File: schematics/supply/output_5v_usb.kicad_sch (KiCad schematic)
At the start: 90 parts, among them J2 USB_A, Q1 40N06, Q2 STP13NK60Z, Q3 STP13NK60Z, U1 INA3221, U10 LM158DR, U11 LM1085-3.3, U2 EL817, U3 MC34063AD, U4 L78L33ACUTR, U5 IRS2153S, U6 LM158DR, U7 IP2163, U8 LM158DR, U9 TL432DBZ

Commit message: Found and fixed issues in schematics.
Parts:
- added R64: 0.01, Resistor_SMD:R_2512_6332Metric, symbol Device:R
- C7: value 0.33 uF -> 10 uF
- C9: value 100 nF -> 10 uF
- R10, R9: value 5 -> 10
- R13, R18, R23, R24: value 1K -> 510
- R6: value 1K -> 50
- U5: value IRS2153S -> IR2153S
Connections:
- net USB_1_+5V: now also R64.1; no longer L1.1, U3.1 (SwC), U3.7 (Ipk), U3.8 (DC)
- new net: L1.1, R64.2, U3.1 (SwC), U3.7 (Ipk), U3.8 (DC)
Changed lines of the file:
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@@
   (junction (at 304.8 33.02) (diameter 0) (color 0 0 0 0)
   )
-  (junction (at 76.2 144.78) (diameter 0) (color 0 0 0 0)
-  )
   (junction (at 85.09 59.69) (diameter 0) (color 0 0 0 0)
   )
@@
   (junction (at 382.27 160.02) (diameter 0) (color 0 0 0 0)
   )
+  (junction (at 76.2 139.7) (diameter 0) (color 0 0 0 0)
+  )
   (junction (at 120.65 193.04) (diameter 0) (color 0 0 0 0)
   )
@@
   (junction (at 187.96 48.26) (diameter 0) (color 0 0 0 0)
   )
+  (junction (at 76.2 142.24) (diameter 0) (color 0 0 0 0)
+  )
   (junction (at 152.4 41.91) (diameter 0) (color 0 0 0 0)
   )
@@
   (junction (at 275.59 48.26) (diameter 0) (color 0 0 0 0)
   )
+  (junction (at 87.63 139.7) (diameter 0) (color 0 0 0 0)
+  )
   (junction (at 337.82 102.87) (diameter 0) (color 0 0 0 0)
   )
@@
   (junction (at 347.98 156.21) (diameter 0) (color 0 0 0 0)
   )
-  (junction (at 87.63 139.7) (diameter 0) (color 0 0 0 0)
-  )
   (junction (at 85.09 45.72) (diameter 0) (color 0 0 0 0)
   )
@@
     (stroke (width 0) (type default))
   )
-  (wire (pts (xy 76.2 139.7) (xy 87.63 139.7))
-    (stroke (width 0) (type default))
-  )
   (wire (pts (xy 31.75 236.22) (xy 36.83 236.22))
     (stroke (width 0) (type default))
@@
     (stroke (width 0) (type default))
   )
+  (wire (pts (xy 76.2 139.7) (xy 76.2 142.24))
+    (stroke (width 0) (type default))
+  )
   (wire (pts (xy 381 64.77) (xy 391.16 64.77))
     (stroke (width 0) (type default))
@@
     (stroke (width 0) (type default))
   )
+  (wire (pts (xy 87.63 137.16) (xy 87.63 139.7))
+    (stroke (width 0) (type default))
+  )
   (wire (pts (xy 113.03 233.68) (xy 113.03 234.95))
     (stroke (width 0) (type default))
@@
     (stroke (width 0) (type default))
   )
-  (wire (pts (xy 87.63 139.7) (xy 97.79 139.7))
+  (wire (pts (xy 76.2 139.7) (xy 87.63 139.7))
     (stroke (width 0) (type default))
   )
@@
     (stroke (width 0) (type default))
   )
-  (wire (pts (xy 76.2 144.78) (xy 80.01 144.78))
-    (stroke (width 0) (type default))
-  )
   (wire (pts (xy 250.19 52.07) (xy 250.19 48.26))
     (stroke (width 0) (type default))
@@
     (stroke (width 0) (type default))
   )
+  (wire (pts (xy 87.63 127) (xy 87.63 129.54))
+    (stroke (width 0) (type default))
+  )
   (wire (pts (xy 388.62 86.36) (xy 388.62 88.9))
     (stroke (width 0) (type default))
@@
     (stroke (width 0) (type default))
   )
+  (wire (pts (xy 87.63 139.7) (xy 97.79 139.7))
+    (stroke (width 0) (type default))
+  )
   (wire (pts (xy 187.96 33.02) (xy 187.96 35.56))
     (stroke (width 0) (type default))
@@
     (stroke (width 0) (type default))
   )
-  (wire (pts (xy 87.63 127) (xy 87.63 139.7))
-    (stroke (width 0) (type default))
-  )
   (wire (pts (xy 121.92 58.42) (xy 125.73 58.42))
     (stroke (width 0) (type default))
@@
     (effects (font (size 1.27 1.27)) (justify right bottom))
   )
-  (label "USB_1_+5V" (at 80.01 144.78 0) (fields_autoplaced)
-    (effects (font (size 1.27 1.27)) (justify left bottom))
-  )
   (hierarchical_label "+5V_OUT" (shape input) (at 31.75 45.72 180) (fields_autoplaced)
     (effects (font (size 1.27 1.27)) (justify right))
@@
       (effects (font (size 1.27 1.27)) (justify left))
     )
-    (property "Value" "IRS2153S" (at 96.52 29.21 0)
+    (property "Value" "IR2153S" (at 96.52 29.21 0)
       (effects (font (size 1.27 1.27)) (justify left))
     )
@@
   (symbol (lib_id "Device:R") (at 129.54 58.42 90) (unit 1)
     (in_bom yes) (on_board yes) (dnp no) (fields_autoplaced)
-    (property "Reference" "R10" (at 129.54 53.34 90)
+    (property "Reference" "R10" (at 129.54 52.07 90)
       (effects (font (size 1.27 1.27)))
     )
-    (property "Value" "5" (at 129.54 55.88 90)
+    (property "Value" "10" (at 129.54 54.61 90)
       (effects (font (size 1.27 1.27)))
     )
@@
       (effects (font (size 1.27 1.27)) (justify right))
     )
-    (property "Value" "0.33 uF" (at 80.01 231.14 0)
+    (property "Value" "10 uF" (at 80.01 231.14 0)
       (effects (font (size 1.27 1.27)) (justify right))
     )
@@
   (symbol (lib_id "Device:R") (at 180.34 260.35 90) (unit 1)
     (in_bom yes) (on_board yes) (dnp no) (fields_autoplaced)
-    (property "Reference" "R13" (at 180.34 255.27 90)
+    (property "Reference" "R13" (at 180.34 254 90)
       (effects (font (size 1.27 1.27)))
     )
-    (property "Value" "1K" (at 180.34 257.81 90)
+    (property "Value" "510" (at 180.34 256.54 90)
       (effects (font (size 1.27 1.27)))
     )
@@
       (effects (font (size 1.27 1.27)) (justify right))
     )
-    (property "Value" "100 nF" (at 116.84 231.14 0)
+    (property "Value" "10 uF" (at 116.84 231.14 0)
       (effects (font (size 1.27 1.27)) (justify right))
     )
@@
   (symbol (lib_id "Device:R") (at 279.4 200.66 90) (unit 1)
     (in_bom yes) (on_board yes) (dnp no) (fields_autoplaced)
-    (property "Reference" "R18" (at 279.4 195.58 90)
+    (property "Reference" "R18" (at 279.4 194.31 90)
       (effects (font (size 1.27 1.27)))
     )
-    (property "Value" "1K" (at 279.4 198.12 90)
+    (property "Value" "510" (at 279.4 196.85 90)
       (effects (font (size 1.27 1.27)))
     )
@@
       (effects (font (size 1.27 1.27)) (justify right))
     )
-    (property "Value" "1K" (at 391.16 93.98 0)
+    (property "Value" "510" (at 391.16 93.98 0)
       (effects (font (size 1.27 1.27)) (justify right))
     )
@@
   (symbol (lib_id "Device:R") (at 129.54 26.67 90) (unit 1)
     (in_bom yes) (on_board yes) (dnp no) (fields_autoplaced)
-    (property "Reference" "R9" (at 129.54 21.59 90)
+    (property "Reference" "R9" (at 129.54 20.32 90)
       (effects (font (size 1.27 1.27)))
     )
-    (property "Value" "5" (at 129.54 24.13 90)
+    (property "Value" "10" (at 129.54 22.86 90)
       (effects (font (size 1.27 1.27)))
     )
@@
   (symbol (lib_id "Device:R") (at 99.06 154.94 0) (unit 1)
     (in_bom yes) (on_board yes) (dnp no) (fields_autoplaced)
-    (property "Reference" "R6" (at 101.6 154.305 0)
+    (property "Reference" "R6" (at 101.6 153.67 0)
       (effects (font (size 1.27 1.27)) (justify left))
     )
-    (property "Value" "1K" (at 101.6 156.845 0)
+    (property "Value" "50" (at 101.6 156.21 0)
       (effects (font (size 1.27 1.27)) (justify left))
     )
@@
     )
   )
+  (symbol (lib_id "Device:R") (at 87.63 133.35 0) (unit 1)
+    (in_bom yes) (on_board yes) (dnp no)
+    (property "Reference" "R64" (at 83.82 132.08 0)
+      (effects (font (size 1.27 1.27)))
+    )
+    (property "Value" "0.01" (at 83.82 134.62 0)
+      (effects (font (size 1.27 1.27)))
+    )
+    (property "Footprint" "Resistor_SMD:R_2512_6332Metric" (at 85.852 133.35 90)
+      (effects (font (size 1.27 1.27)) hide)
+    )
+    (property "Datasheet" "~" (at 87.63 133.35 0)
+      (effects (font (size 1.27 1.27)) hide)
+    )
+    (pin "1")
+    (pin "2")
+    (instances
+      (project "supply"
+        (path "/1e139717-fcd1-4008-a6ea-4c993845e928/bcabd54f-a555-4409-9a4f-89c20a3d7682"
+          (reference "R64") (unit 1)
+        )
+      )
+    )
+  )
   (symbol (lib_id "power:GND") (at 275.59 101.6 0) (unit 1)
     (in_bom yes) (on_board yes) (dnp no) (fields_autoplaced)
@@
   (symbol (lib_id "Device:R") (at 350.52 200.66 90) (unit 1)
     (in_bom yes) (on_board yes) (dnp no) (fields_autoplaced)
-    (property "Reference" "R23" (at 350.52 195.58 90)
+    (property "Reference" "R23" (at 350.52 194.31 90)
       (effects (font (size 1.27 1.27)))
     )
-    (property "Value" "1K" (at 350.52 198.12 90)
+    (property "Value" "510" (at 350.52 196.85 90)
       (effects (font (size 1.27 1.27)))
     )

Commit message: Some changes
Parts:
- C4: value 100 nF -> 1 uF
- R1: value 510 -> 120
- R17: value 10K -> 3K3
- R2: value 1K2 -> NOT INSTALLED
- R6: value 50 -> 51
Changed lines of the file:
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@@
       (effects (font (size 1.27 1.27)) (justify right))
     )
-    (property "Value" "1K2" (at 50.8 53.34 0)
+    (property "Value" "NOT INSTALLED" (at 50.8 53.34 0)
       (effects (font (size 1.27 1.27)) (justify right))
     )
@@
       (effects (font (size 1.27 1.27)) (justify left))
     )
-    (property "Value" "10K" (at 278.13 93.98 0)
+    (property "Value" "3K3" (at 278.13 93.98 0)
       (effects (font (size 1.27 1.27)) (justify left))
     )
@@
       (effects (font (size 1.27 1.27) italic) hide)
     )
-    (property "Datasheet" "http://www.ti.com/lit/ds/symlink/lm1085.pdf" (at 353.06 102.87 0)
+    (property "Datasheet" "https://static.chipdip.ru/lib/142/DOC000142627.pdf" (at 353.06 102.87 0)
       (effects (font (size 1.27 1.27)) hide)
     )
@@
   (symbol (lib_id "Device:R") (at 39.37 45.72 270) (mirror x) (unit 1)
     (in_bom yes) (on_board yes) (dnp no) (fields_autoplaced)
-    (property "Reference" "R1" (at 39.37 40.64 90)
-      (effects (font (size 1.27 1.27)))
-    )
-    (property "Value" "510" (at 39.37 43.18 90)
+    (property "Reference" "R1" (at 39.37 39.37 90)
+      (effects (font (size 1.27 1.27)))
+    )
+    (property "Value" "120" (at 39.37 41.91 90)
       (effects (font (size 1.27 1.27)))
     )
@@
       (effects (font (size 1.27 1.27)) (justify left))
     )
-    (property "Value" "50" (at 101.6 156.21 0)
+    (property "Value" "51" (at 101.6 156.21 0)
       (effects (font (size 1.27 1.27)) (justify left))
     )
@@
       (effects (font (size 1.27 1.27)) (justify right))
     )
-    (property "Value" "100 nF" (at 74.93 26.67 0)
+    (property "Value" "1 uF" (at 74.93 26.67 0)
       (effects (font (size 1.27 1.27)) (justify right))
     )
@@
       (effects (font (size 1.27 1.27)) hide)
     )
-    (property "Datasheet" "~" (at 204.47 48.26 0)
-      (effects (font (size 1.27 1.27)) hide)
-    )
+    (property "Datasheet" "https://static.chipdip.ru/lib/926/DOC012926706.pdf" (at 204.47 48.26 0)
+      (effects (font (size 1.27 1.27)) hide)
+    )

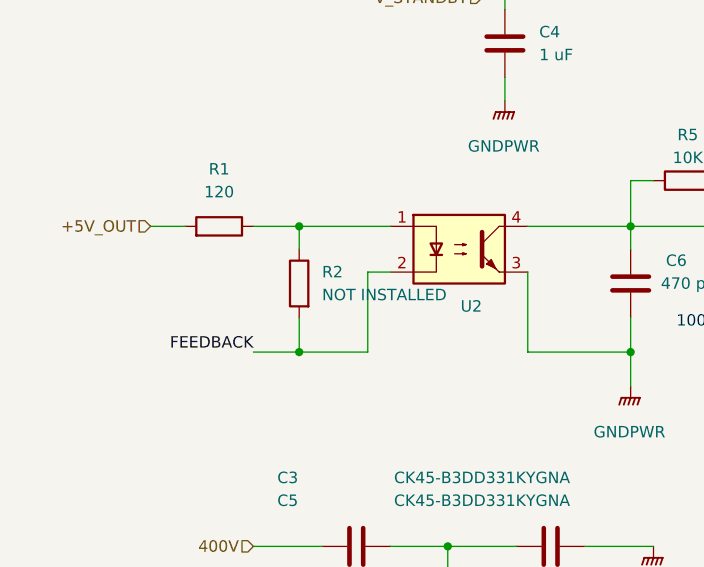
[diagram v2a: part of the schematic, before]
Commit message: fix pins in firmware
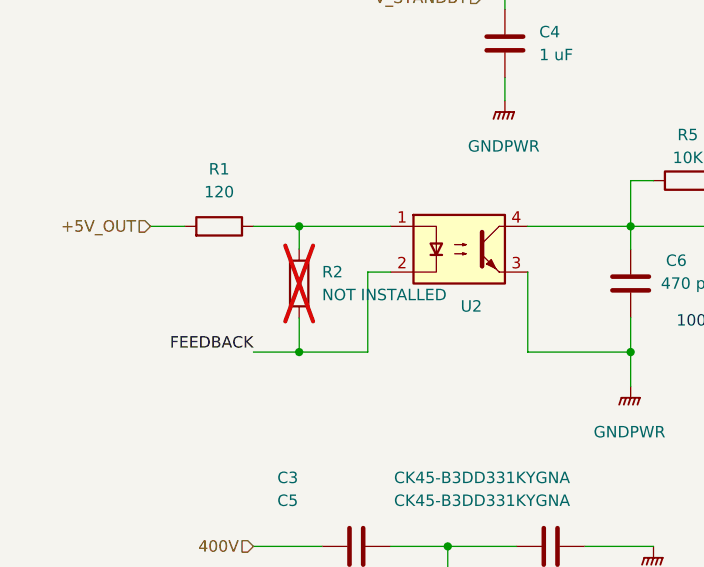
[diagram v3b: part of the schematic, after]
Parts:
- R2: now not fitted
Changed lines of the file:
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@@
   )
   (symbol (lib_id "Device:R") (at 48.26 52.07 0) (mirror y) (unit 1)
-    (in_bom yes) (on_board yes) (dnp no) (fields_autoplaced)
+    (in_bom yes) (on_board yes) (dnp yes) (fields_autoplaced)
     (property "Reference" "R2" (at 50.8 50.8 0)
       (effects (font (size 1.27 1.27)) (justify right))

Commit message: Continue soldering and setting up hardware
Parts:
- D16: value SS16 -> STTH1R06A
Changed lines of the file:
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@@
   (symbol (lib_id "Device:D") (at 115.57 26.67 180) (unit 1)
     (in_bom yes) (on_board yes) (dnp no) (fields_autoplaced)
-    (property "Reference" "D16" (at 115.57 21.59 0)
+    (property "Reference" "D16" (at 115.57 20.32 0)
       (effects (font (size 1.27 1.27)))
     )
-    (property "Value" "SS16" (at 115.57 24.13 0)
+    (property "Value" "STTH1R06A" (at 115.57 22.86 0)
       (effects (font (size 1.27 1.27)))
     )

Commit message: Board fixes
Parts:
- added R65, R66: 0.07, Resistor_SMD:R_2512_6332Metric, symbol Device:R
- R64: value 0.01 -> 0.07
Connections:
- net USB_1_+5V: now also R65.1, R66.1
- net at L1.1, R64.2, U3.1 (SwC)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: now also R65.2, R66.2
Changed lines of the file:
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@@
   (junction (at 158.75 142.24) (diameter 0) (color 0 0 0 0)
   )
+  (junction (at 91.44 128.27) (diameter 0) (color 0 0 0 0)
+  )
   (junction (at 99.06 149.86) (diameter 0) (color 0 0 0 0)
   )
@@
   (junction (at 85.09 59.69) (diameter 0) (color 0 0 0 0)
   )
+  (junction (at 87.63 128.27) (diameter 0) (color 0 0 0 0)
+  )
   (junction (at 327.66 140.97) (diameter 0) (color 0 0 0 0)
   )
@@
   (junction (at 347.98 156.21) (diameter 0) (color 0 0 0 0)
   )
+  (junction (at 87.63 138.43) (diameter 0) (color 0 0 0 0)
+  )
   (junction (at 85.09 45.72) (diameter 0) (color 0 0 0 0)
   )
   (junction (at 187.96 49.53) (diameter 0) (color 0 0 0 0)
   )
+  (junction (at 91.44 138.43) (diameter 0) (color 0 0 0 0)
+  )
   (junction (at 129.54 142.24) (diameter 0) (color 0 0 0 0)
   )
@@
     (stroke (width 0) (type default))
   )
+  (wire (pts (xy 91.44 138.43) (xy 87.63 138.43))
+    (stroke (width 0) (type default))
+  )
   (wire (pts (xy 90.17 224.79) (xy 93.98 224.79))
     (stroke (width 0) (type default))
@@
     (stroke (width 0) (type default))
   )
+  (wire (pts (xy 91.44 128.27) (xy 87.63 128.27))
+    (stroke (width 0) (type default))
+  )
   (wire (pts (xy 304.8 39.37) (xy 322.58 39.37))
     (stroke (width 0) (type default))
@@
     (stroke (width 0) (type default))
   )
-  (wire (pts (xy 87.63 137.16) (xy 87.63 139.7))
+  (wire (pts (xy 87.63 137.16) (xy 87.63 138.43))
     (stroke (width 0) (type default))
   )
@@
     (stroke (width 0) (type default))
   )
+  (wire (pts (xy 95.25 129.54) (xy 95.25 128.27))
+    (stroke (width 0) (type default))
+  )
   (wire (pts (xy 234.95 110.49) (xy 234.95 114.3))
     (stroke (width 0) (type default))
@@
     (stroke (width 0) (type default))
   )
+  (wire (pts (xy 87.63 138.43) (xy 87.63 139.7))
+    (stroke (width 0) (type default))
+  )
   (wire (pts (xy 156.21 201.93) (xy 158.75 201.93))
     (stroke (width 0) (type default))
@@
     (stroke (width 0) (type default))
   )
+  (wire (pts (xy 95.25 138.43) (xy 91.44 138.43))
+    (stroke (width 0) (type default))
+  )
   (wire (pts (xy 62.23 248.92) (xy 67.31 248.92))
     (stroke (width 0) (type default))
@@
     (stroke (width 0) (type default))
   )
+  (wire (pts (xy 95.25 137.16) (xy 95.25 138.43))
+    (stroke (width 0) (type default))
+  )
   (wire (pts (xy 73.66 45.72) (xy 85.09 45.72))
     (stroke (width 0) (type default))
@@
     (stroke (width 0) (type default))
   )
-  (wire (pts (xy 87.63 127) (xy 87.63 129.54))
+  (wire (pts (xy 87.63 127) (xy 87.63 128.27))
     (stroke (width 0) (type default))
   )
@@
     (stroke (width 0) (type default))
   )
+  (wire (pts (xy 91.44 137.16) (xy 91.44 138.43))
+    (stroke (width 0) (type default))
+  )
   (wire (pts (xy 109.22 26.67) (xy 111.76 26.67))
     (stroke (width 0) (type default))
@@
     (stroke (width 0) (type default))
   )
+  (wire (pts (xy 91.44 129.54) (xy 91.44 128.27))
+    (stroke (width 0) (type default))
+  )
   (wire (pts (xy 360.68 102.87) (xy 367.03 102.87))
     (stroke (width 0) (type default))
@@
     (stroke (width 0) (type default))
   )
+  (wire (pts (xy 87.63 128.27) (xy 87.63 129.54))
+    (stroke (width 0) (type default))
+  )
   (wire (pts (xy 229.87 114.3) (xy 223.52 114.3))
     (stroke (width 0) (type default))
@@
     (stroke (width 0) (type default))
   )
+  (wire (pts (xy 95.25 128.27) (xy 91.44 128.27))
+    (stroke (width 0) (type default))
+  )
   (wire (pts (xy 121.92 58.42) (xy 125.73 58.42))
     (stroke (width 0) (type default))
@@
     )
   )
+  (symbol (lib_id "Device:R") (at 95.25 133.35 0) (unit 1)
+    (in_bom yes) (on_board yes) (dnp no)
+    (property "Reference" "R66" (at 77.47 137.16 0)
+      (effects (font (size 1.27 1.27)))
+    )
+    (property "Value" "0.07" (at 82.55 137.16 0)
+      (effects (font (size 1.27 1.27)))
+    )
+    (property "Footprint" "Resistor_SMD:R_2512_6332Metric" (at 93.472 133.35 90)
+      (effects (font (size 1.27 1.27)) hide)
+    )
+    (property "Datasheet" "~" (at 95.25 133.35 0)
+      (effects (font (size 1.27 1.27)) hide)
+    )
+    (pin "1")
+    (pin "2")
+    (instances
+      (project "supply"
+        (path "/1e139717-fcd1-4008-a6ea-4c993845e928/bcabd54f-a555-4409-9a4f-89c20a3d7682"
+          (reference "R66") (unit 1)
+        )
+      )
+    )
+  )
   (symbol (lib_id "power:GND") (at 250.19 63.5 0) (unit 1)
     (in_bom yes) (on_board yes) (dnp no) (fields_autoplaced)
@@
     )
   )
+  (symbol (lib_id "Device:R") (at 91.44 133.35 0) (unit 1)
+    (in_bom yes) (on_board yes) (dnp no)
+    (property "Reference" "R65" (at 77.47 134.62 0)
+      (effects (font (size 1.27 1.27)))
+    )
+    (property "Value" "0.07" (at 82.55 134.62 0)
+      (effects (font (size 1.27 1.27)))
+    )
+    (property "Footprint" "Resistor_SMD:R_2512_6332Metric" (at 89.662 133.35 90)
+      (effects (font (size 1.27 1.27)) hide)
+    )
+    (property "Datasheet" "~" (at 91.44 133.35 0)
+      (effects (font (size 1.27 1.27)) hide)
+    )
+    (pin "1")
+    (pin "2")
+    (instances
+      (project "supply"
+        (path "/1e139717-fcd1-4008-a6ea-4c993845e928/bcabd54f-a555-4409-9a4f-89c20a3d7682"
+          (reference "R65") (unit 1)
+        )
+      )
+    )
+  )
   (symbol (lib_id "power:GND") (at 388.62 100.33 0) (unit 1)
     (in_bom yes) (on_board yes) (dnp no) (fields_autoplaced)
@@
   (symbol (lib_id "Device:R") (at 87.63 133.35 0) (unit 1)
     (in_bom yes) (on_board yes) (dnp no)
-    (property "Reference" "R64" (at 83.82 132.08 0)
+    (property "Reference" "R64" (at 77.47 132.08 0)
       (effects (font (size 1.27 1.27)))
     )
-    (property "Value" "0.01" (at 83.82 134.62 0)
+    (property "Value" "0.07" (at 82.55 132.08 0)
       (effects (font (size 1.27 1.27)))
     )
